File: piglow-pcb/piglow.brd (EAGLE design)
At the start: 36.8 x 33.7 mm, 30 parts, among them IC1 ic-sm3218-qfn24, P1 led-pink-0805, P2 led-pink-0805, P3 led-pink-0805, Y1 led-yellow-0805, Y2 led-yellow-0805, Y3 led-yellow-0805

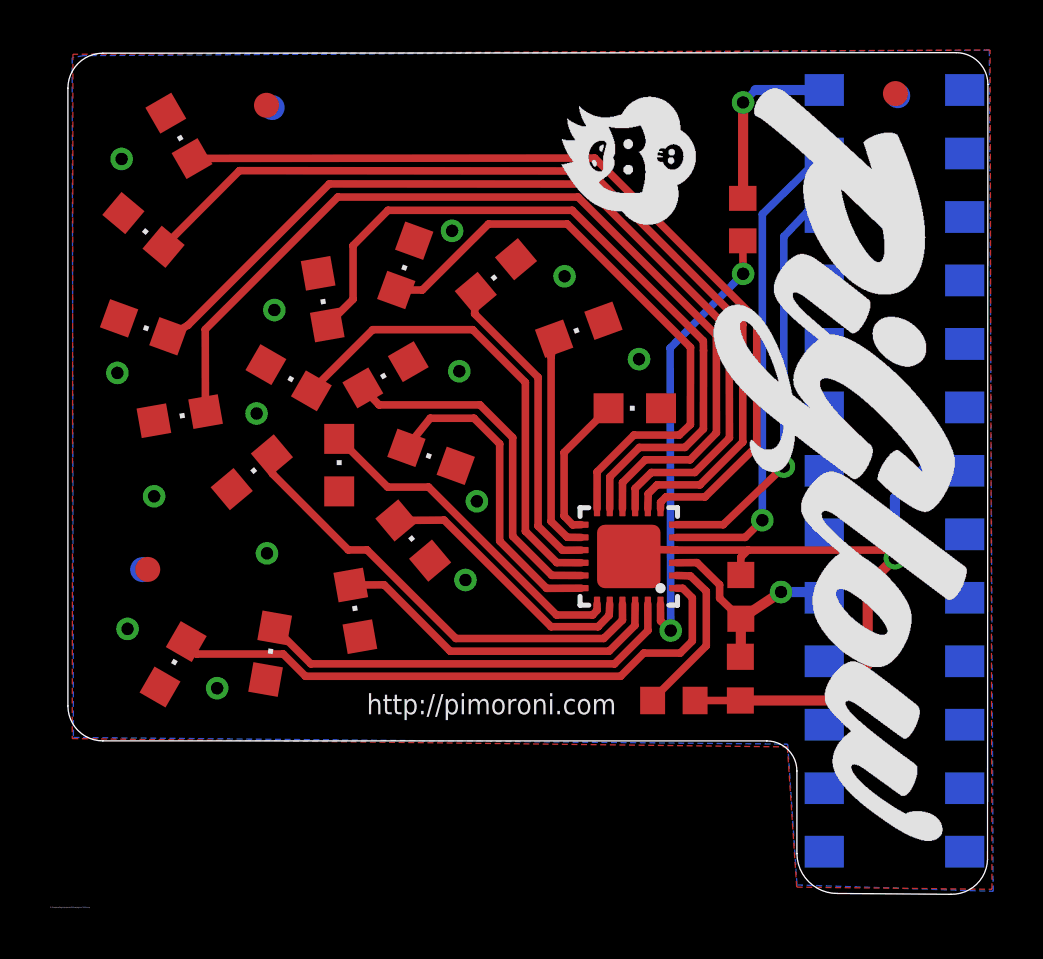
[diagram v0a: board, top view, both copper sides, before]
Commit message: New SN3218 landing
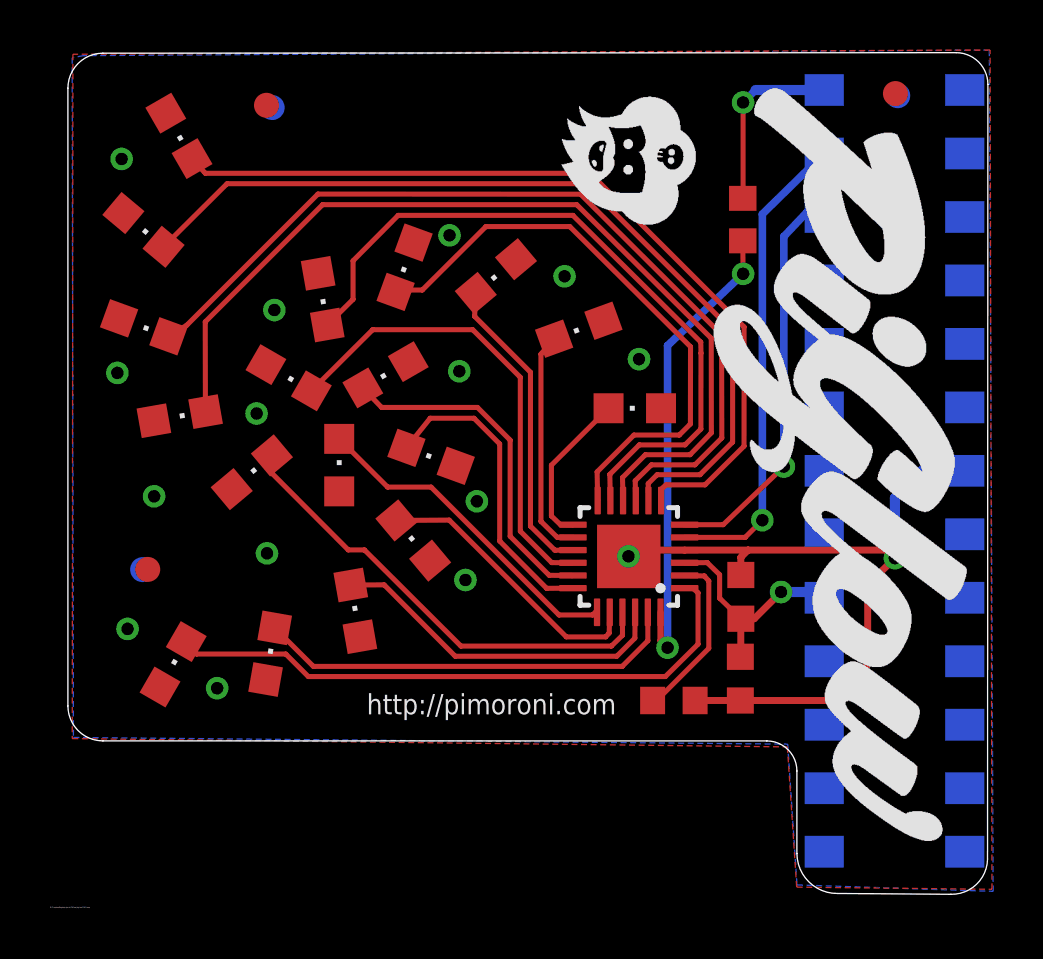
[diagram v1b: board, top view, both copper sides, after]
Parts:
- moved G3 0.08 mm to (14.2, 25.5)
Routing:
- net N$8: track 35.7 -> 34.2 mm
- net N$9: track 36.9 -> 35.4 mm
- net N$10: track 37.1 -> 35.9 mm
- net N$3: track 18.0 -> 19.1 mm
- net N$12: track 29.7 -> 28.7 mm
- net N$11: track 37.8 -> 37.0 mm
